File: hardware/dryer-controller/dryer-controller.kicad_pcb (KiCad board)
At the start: 2 copper layers, 110 x 85 mm, 69 parts, among them K1 SRD-05VDC-SL-C, K2 SRD-05VDC-SL-C, Q1 MMBT2222A, Q2 MMBT2222A, Q3 CJ2310, Q4 CJ2310, Q5 CJ2310, SW1 SW-USB, U1 K7805-1000R3

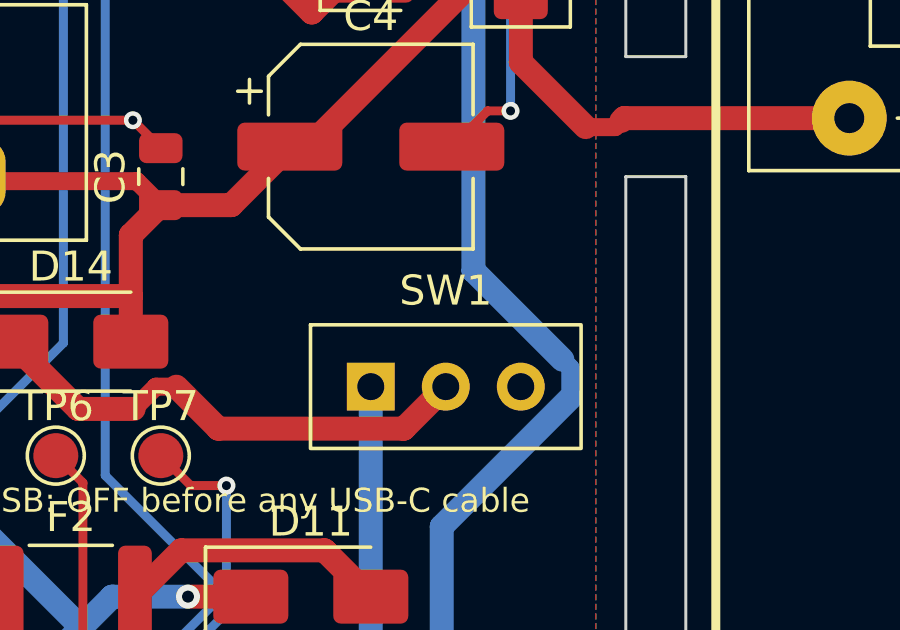
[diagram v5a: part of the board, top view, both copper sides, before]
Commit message: Add SW-USB ON/OFF legends and fix review points in the PCB check
The continuity check told the technician to find the ON position on the
silkscreen, but the board had only the "OFF before any USB-C" line. Add
"ON" (above pin 1) and "OFF" (above pin 3) legends at SW1, regenerate
the board and review files (DRC 0 violations, 0 unconnected), and define
OFF electrically in the check.

Item 4 claimed the 6-pin loads plug cannot enter J_MAINS; both are
5.08 mm, so it can. Drop that row and say so in hardware.md. Also make
the 12-pin 3 drop reading ESP-in only, simplify the coil row, drop the
duplicate D11 row, state the item 7 power state and the J_24V probe
polarity.

Co-Authored-By: Claude Sonnet 5.5 <noreply@anthropic.com>
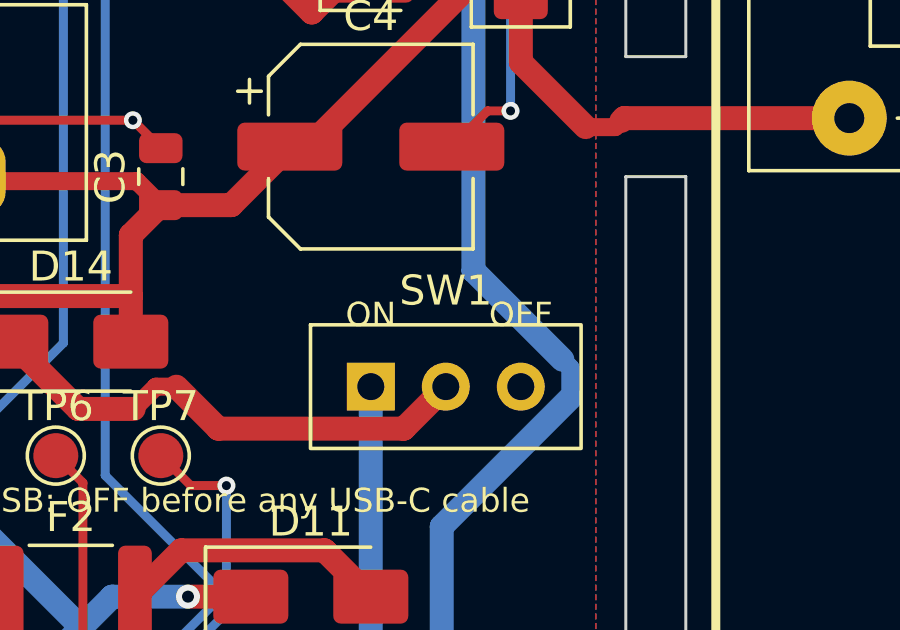
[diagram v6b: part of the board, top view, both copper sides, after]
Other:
- board text added: "OFF"
- board text added: "ON"
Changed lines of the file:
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@@
+		)
+	)
+	(gr_text "ON"
+		(at 62 34.6 0)
+		(layer "F.SilkS")
+		(effects
+			(font
+				(size 0.8 0.8)
+				(thickness 0.12)
+			)
+		)
+	)
+	(gr_text "OFF"
+		(at 67 34.6 0)
+		(layer "F.SilkS")
+		(effects
+			(font
+				(size 0.8 0.8)
+				(thickness 0.12)
+			)
 		)
 	)
